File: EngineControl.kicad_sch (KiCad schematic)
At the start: 0 parts

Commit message: Complete Rev0
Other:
- added sheet Ignition (ignition.kicad_sch)
- added sheet MCU (mcu.kicad_sch)
- added sheet Power Delivery (power.kicad_sch)
- note added: "JLCPCB: JLC7628 Track Width Space Configuration DIFF90 6.89mil 4mil DIFF100 4.96mil 4mil DIFF120 4.97mil 8mil SE60 7.93mil N/A"
- company: (none) -> Badger
- title: (none) -> Badger-Pike: Engine Control Module

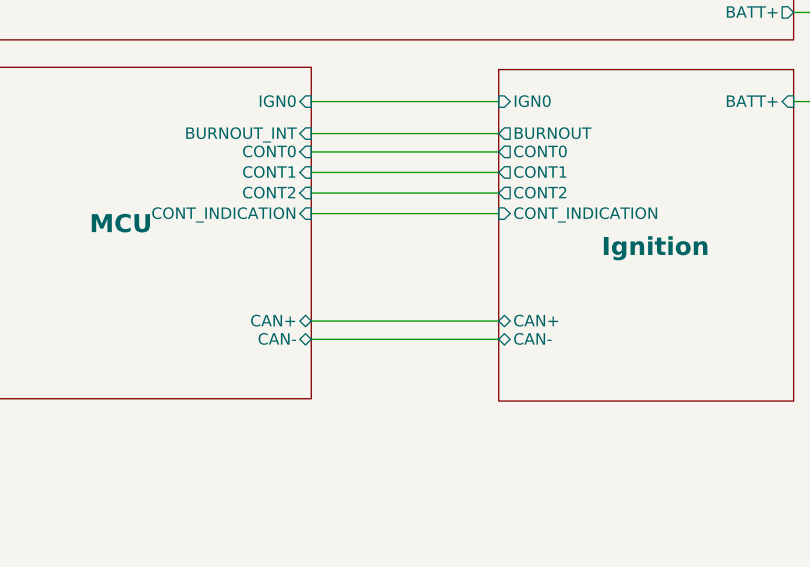
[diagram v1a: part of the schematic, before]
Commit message: Update ignition system with CDI
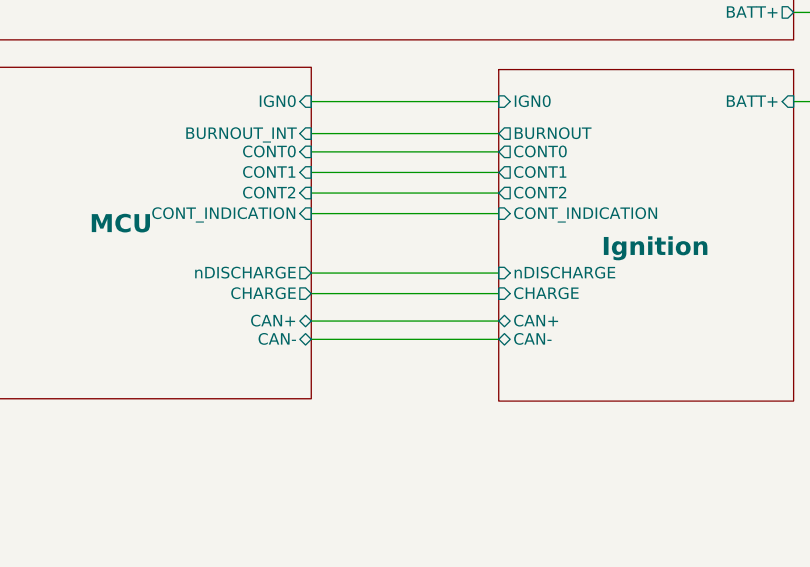
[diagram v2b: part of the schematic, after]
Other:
- sheet Ignition ports: added CHARGE, nDISCHARGE; removed none
- sheet MCU ports: added CHARGE, nDISCHARGE; removed none
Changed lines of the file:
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@@
+    (stroke (width 0) (type solid) (color 0 0 0 0))
+  )
+  (wire (pts (xy 142.24 77.47) (xy 163.068 77.47))
+    (stroke (width 0) (type solid) (color 0 0 0 0))
+  )
+  (wire (pts (xy 142.24 79.756) (xy 163.068 79.756))
     (stroke (width 0) (type solid) (color 0 0 0 0))
   )
@@
       (effects (font (size 1.27 1.27)) (justify left))
     )
+    (pin "nDISCHARGE" input (at 163.068 77.47 180)
+      (effects (font (size 1.27 1.27)) (justify left))
+    )
+    (pin "CHARGE" input (at 163.068 79.756 180)
+      (effects (font (size 1.27 1.27)) (justify left))
+    )
   )
   (sheet (at 102.108 54.61) (size 40.132 36.83)
@@
       (effects (font (size 1.27 1.27)) (justify right))
     )
+    (pin "nDISCHARGE" output (at 142.24 77.47 0)
+      (effects (font (size 1.27 1.27)) (justify right))
+    )
+    (pin "CHARGE" output (at 142.24 79.756 0)
+      (effects (font (size 1.27 1.27)) (justify right))
+    )
   )
   (sheet (at 101.854 34.544) (size 93.98 17.018)
@@
       (reference "#PWR021") (unit 1) (value "GND") (footprint "")
     )
+    (path "/021a2ddc-ba8f-4bf6-8fd4-c966327b4dd3/11e8ddb4-d444-4e7a-9a9e-5be1caf13b32"
+      (reference "#PWR?") (unit 1) (value "GND") (footprint "")
+    )
+    (path "/021a2ddc-ba8f-4bf6-8fd4-c966327b4dd3/169c89da-08f3-4afe-9e1c-06ef9693fbdb"
+      (reference "#PWR?") (unit 1) (value "GND") (footprint "")
+    )
+    (path "/021a2ddc-ba8f-4bf6-8fd4-c966327b4dd3/e03192f3-1f54-4a91-a410-de67ec52ca15"
+      (reference "#PWR?") (unit 1) (value "GND") (footprint "")
+    )
+    (path "/021a2ddc-ba8f-4bf6-8fd4-c966327b4dd3/fc22141e-0464-4c9b-a99c-9164e34aa44a"
+      (reference "#PWR?") (unit 1) (value "GND") (footprint "")
+    )
     (path "/472485e8-070c-45e8-970c-81997ac9d31f/9a635782-a656-4901-a321-decefa99a249"
       (reference "C1") (unit 1) (value "10uF") (footprint "Capacitor_Tantalum_SMD:CP_EIA-3216-18_Kemet-A")
@@
       (reference "C12") (unit 1) (value "100u") (footprint "Capacitor_Tantalum_SMD:CP_EIA-7343-31_Kemet-D")
     )
+    (path "/021a2ddc-ba8f-4bf6-8fd4-c966327b4dd3/e51a0524-21e2-417c-9e03-1e8f9e98a4c8"
+      (reference "C?") (unit 1) (value "2000uF") (footprint "")
+    )
     (path "/472485e8-070c-45e8-970c-81997ac9d31f/f9e04ee8-79d0-4648-81f5-c705e65b0835"
       (reference "D1") (unit 1) (value "LED_HeartBeat") (footprint "LED_SMD:LED_0603_1608Metric")
@@
       (reference "D3") (unit 1) (value "LED_Cont.") (footprint "LED_SMD:LED_0603_1608Metric")
     )
+    (path "/021a2ddc-ba8f-4bf6-8fd4-c966327b4dd3/529cc0e4-e45f-47f5-99e7-e39d73786a12"
+      (reference "D?") (unit 1) (value "LED_Charge") (footprint "LED_SMD:LED_0603_1608Metric")
+    )
+    (path "/021a2ddc-ba8f-4bf6-8fd4-c966327b4dd3/65e1a0d3-06ad-4d06-8248-bcd9e5015372"
+      (reference "D?") (unit 1) (value "LED_Discharge") (footprint "LED_SMD:LED_0603_1608Metric")
+    )
     (path "/472485e8-070c-45e8-970c-81997ac9d31f/f613bc73-f435-40ba-8cd6-0bc925e3ec73"
       (reference "FB1") (unit 1) (value "180 @ 100 Mhz") (footprint "Inductor_SMD:L_0603_1608Metric_Pad1.05x0.95mm_HandSolder")
@@
       (reference "L1") (unit 1) (value "4.7uH") (footprint "Inductor_SMD:L_Vishay_IHLP-1616")
     )
-    (path "/021a2ddc-ba8f-4bf6-8fd4-c966327b4dd3/f7481350-055a-4cee-b1b4-0fd602203b0e"
-      (reference "Q1") (unit 1) (value "Q_NMOS_GDS") (footprint "Package_TO_SOT_SMD:TO-263-3_TabPin2")
+    (path "/021a2ddc-ba8f-4bf6-8fd4-c966327b4dd3/9c8bf34f-46ee-48be-a480-69c389b9c0c8"
+      (reference "Q?") (unit 1) (value "Q_NMOS_GSD") (footprint "")
+    )
+    (path "/021a2ddc-ba8f-4bf6-8fd4-c966327b4dd3/f6891a3a-e048-46eb-bfc6-a9efdf878e9c"
+      (reference "Q?") (unit 1) (value "Q_NMOS_GSD") (footprint "")
     )
     (path "/472485e8-070c-45e8-970c-81997ac9d31f/6c7965de-69af-4ed2-ad27-cfe8a2e8bbc9"
@@
       (reference "R8") (unit 1) (value "1.5k") (footprint "Resistor_SMD:R_0402_1005Metric")
     )
-    (path "/021a2ddc-ba8f-4bf6-8fd4-c966327b4dd3/691f076b-c2f4-4e60-b380-21e64c3d310f"
-      (reference "R9") (unit 1) (value "220R") (footprint "Resistor_SMD:R_0402_1005Metric")
-    )
     (path "/021a2ddc-ba8f-4bf6-8fd4-c966327b4dd3/43e702a9-3533-4715-872a-827af84038be"
       (reference "R10") (unit 1) (value "1.5k") (footprint "Resistor_SMD:R_0402_1005Metric")
     )
+    (path "/021a2ddc-ba8f-4bf6-8fd4-c966327b4dd3/6f4b4f8f-5e59-4384-b394-dfa35396f290"
+      (reference "R?") (unit 1) (value "220R") (footprint "Resistor_SMD:R_0402_1005Metric")
+    )
+    (path "/021a2ddc-ba8f-4bf6-8fd4-c966327b4dd3/96c2e04e-9621-4953-811a-55f9cdbe47fe"
+      (reference "R?") (unit 1) (value "1.5k") (footprint "Resistor_SMD:R_0402_1005Metric")
+    )
+    (path "/021a2ddc-ba8f-4bf6-8fd4-c966327b4dd3/aa5dacce-ba6b-4ac3-8791-dce9d3bf9801"
+      (reference "R?") (unit 1) (value "220R") (footprint "Resistor_SMD:R_0402_1005Metric")
+    )
+    (path "/021a2ddc-ba8f-4bf6-8fd4-c966327b4dd3/e0571af3-4030-489e-8820-d86b2c375277"
+      (reference "R?") (unit 1) (value "1.5k") (footprint "Resistor_SMD:R_0402_1005Metric")
+    )
     (path "/472485e8-070c-45e8-970c-81997ac9d31f/e33953b3-4690-457f-b360-b7b9438ebddd"
       (reference "SW1") (unit 1) (value "BOOT") (footprint "Button_Switch_SMD:SW_DIP_SPSTx01_Slide_6.7x4.1mm_W6.73mm_P2.54mm_LowProfile_JPin")
@@
       (reference "U3") (unit 1) (value "AMS1117-3.3") (footprint "Package_TO_SOT_SMD:SOT-223-3_TabPin2")
     )
+    (path "/021a2ddc-ba8f-4bf6-8fd4-c966327b4dd3/e34a8f98-12ae-4dbb-a4e3-f354e5e27361"
+      (reference "U?") (unit 1) (value "CPC1135N") (footprint "Package_SO:SOP-4_3.8x4.1mm_P2.54mm")
+    )
     (path "/472485e8-070c-45e8-970c-81997ac9d31f/d4047988-d8c1-45f8-8d91-6d57e08950fe"

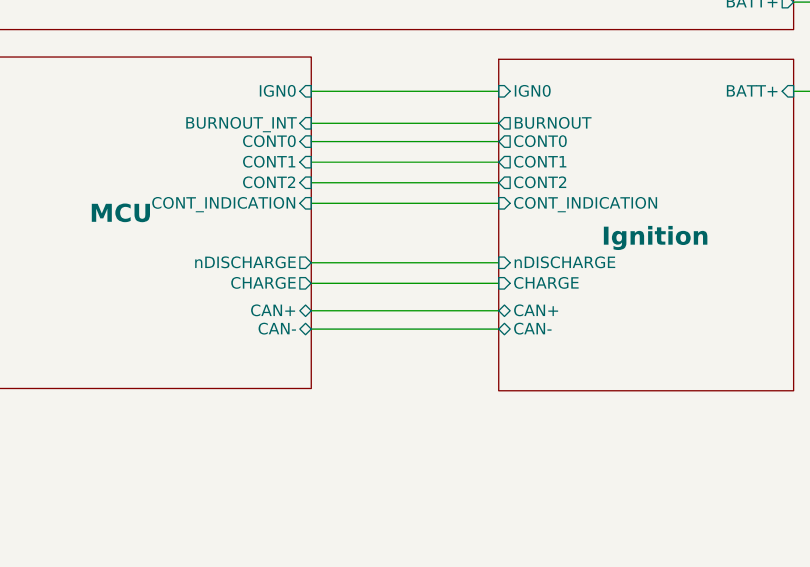
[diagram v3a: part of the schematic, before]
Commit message: #4 add pchannel for charge and nchannel for ignition
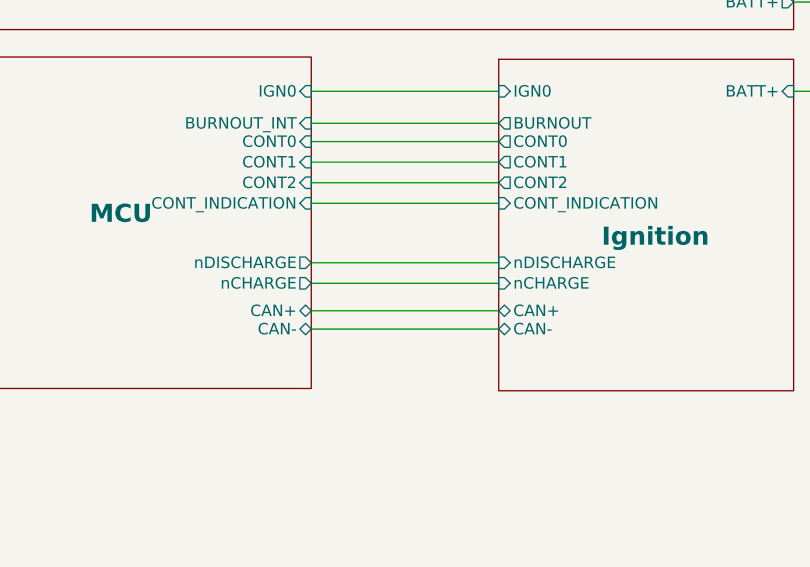
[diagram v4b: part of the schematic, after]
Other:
- sheet Ignition ports: added nCHARGE; removed CHARGE
- sheet MCU ports: added nCHARGE; removed CHARGE
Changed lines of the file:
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@@
       (effects (font (size 1.27 1.27)) (justify left))
     )
-    (pin "CHARGE" input (at 163.068 79.756 180)
+    (pin "nCHARGE" input (at 163.068 79.756 180)
       (effects (font (size 1.27 1.27)) (justify left))
     )
@@
       (effects (font (size 1.27 1.27)) (justify right))
     )
-    (pin "CHARGE" output (at 142.24 79.756 0)
+    (pin "nCHARGE" output (at 142.24 79.756 0)
       (effects (font (size 1.27 1.27)) (justify right))
     )
@@
       (reference "#PWR018") (unit 1) (value "GND") (footprint "")
     )
-    (path "/021a2ddc-ba8f-4bf6-8fd4-c966327b4dd3/66179501-8feb-443f-87b7-69728ec20e47"
+    (path "/021a2ddc-ba8f-4bf6-8fd4-c966327b4dd3/03958684-76a2-4a2e-904e-5f052f038332"
       (reference "#PWR019") (unit 1) (value "GND") (footprint "")
     )
@@
       (reference "#PWR021") (unit 1) (value "GND") (footprint "")
     )
-    (path "/021a2ddc-ba8f-4bf6-8fd4-c966327b4dd3/11e8ddb4-d444-4e7a-9a9e-5be1caf13b32"
-      (reference "#PWR022") (unit 1) (value "GND") (footprint "")
-    )
     (path "/021a2ddc-ba8f-4bf6-8fd4-c966327b4dd3/169c89da-08f3-4afe-9e1c-06ef9693fbdb"
       (reference "#PWR023") (unit 1) (value "GND") (footprint "")
@@
       (reference "L1") (unit 1) (value "4.7uH") (footprint "Inductor_SMD:L_Vishay_IHLP-1616")
     )
-    (path "/021a2ddc-ba8f-4bf6-8fd4-c966327b4dd3/f6891a3a-e048-46eb-bfc6-a9efdf878e9c"
-      (reference "Q1") (unit 1) (value "Q_NMOS_GSD") (footprint "Package_TO_SOT_SMD:SOT-23")
+    (path "/021a2ddc-ba8f-4bf6-8fd4-c966327b4dd3/b441a99b-7eb6-454c-8efc-1e30abb5c3e1"
+      (reference "Q1") (unit 1) (value "PMOS-GSD") (footprint "Package_TO_SOT_SMD:SOT-23")
     )
     (path "/021a2ddc-ba8f-4bf6-8fd4-c966327b4dd3/9c8bf34f-46ee-48be-a480-69c389b9c0c8"
@@
       (reference "R10") (unit 1) (value "1.5k") (footprint "Resistor_SMD:R_0402_1005Metric")
     )
-    (path "/021a2ddc-ba8f-4bf6-8fd4-c966327b4dd3/6f4b4f8f-5e59-4384-b394-dfa35396f290"
-      (reference "R11") (unit 1) (value "220R") (footprint "Resistor_SMD:R_0402_1005Metric")
+    (path "/021a2ddc-ba8f-4bf6-8fd4-c966327b4dd3/7158ea03-02b2-4ce0-90c1-0e3093223193"
+      (reference "R11") (unit 1) (value "100k") (footprint "")
     )
     (path "/021a2ddc-ba8f-4bf6-8fd4-c966327b4dd3/96c2e04e-9621-4953-811a-55f9cdbe47fe"
@@
       (reference "R13") (unit 1) (value "220R") (footprint "Resistor_SMD:R_0402_1005Metric")
     )
+    (path "/021a2ddc-ba8f-4bf6-8fd4-c966327b4dd3/1c8d51e0-1f2b-4f95-85d6-d9e259006f9d"
+      (reference "R14") (unit 1) (value "1.5k") (footprint "Resistor_SMD:R_0402_1005Metric")
+    )
     (path "/472485e8-070c-45e8-970c-81997ac9d31f/e33953b3-4690-457f-b360-b7b9438ebddd"

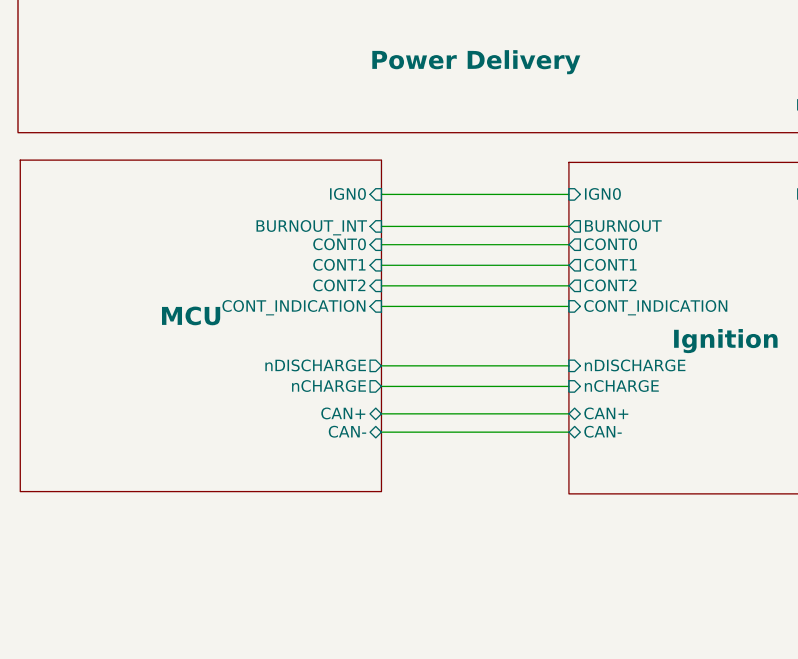
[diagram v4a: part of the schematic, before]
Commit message: #1 New pyro channel introduced in schematic
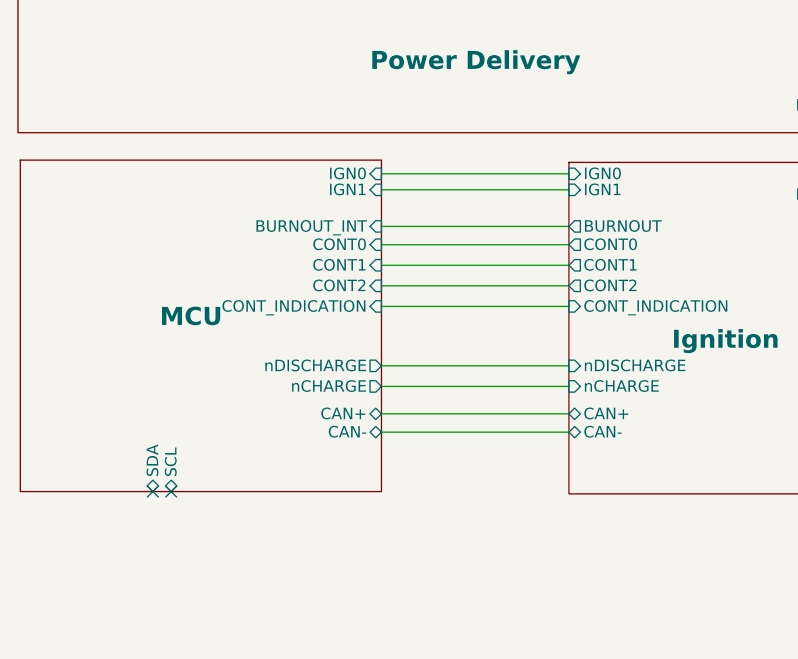
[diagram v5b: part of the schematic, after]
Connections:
- no-connect marks 0 -> 2
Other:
- sheet Ignition ports: added IGN1; removed none
- sheet MCU ports: added IGN1, SCL, SDA; removed none
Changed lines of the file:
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@@
     (company "Badger")
   )
-  (wire (pts (xy 142.24 58.42) (xy 163.068 58.42))
+  (no_connect (at 116.84 91.44))
+  (no_connect (at 118.872 91.44))
+  (wire (pts (xy 142.24 56.134) (xy 163.068 56.134))
+    (stroke (width 0) (type solid) (color 0 0 0 0))
+  )
+  (wire (pts (xy 142.24 57.912) (xy 163.068 57.912))
     (stroke (width 0) (type solid) (color 0 0 0 0))
   )
@@
       (effects (font (size 1.27 1.27)) (justify right))
     )
-    (pin "IGN0" input (at 163.068 58.42 180)
+    (pin "IGN0" input (at 163.068 56.134 180)
       (effects (font (size 1.27 1.27)) (justify left))
     )
@@
     )
     (pin "nCHARGE" input (at 163.068 79.756 180)
+      (effects (font (size 1.27 1.27)) (justify left))
+    )
+    (pin "IGN1" input (at 163.068 57.912 180)
       (effects (font (size 1.27 1.27)) (justify left))
     )
@@
       (effects (font (size 1.27 1.27)) (justify right))
     )
-    (pin "IGN0" input (at 142.24 58.42 0)
+    (pin "IGN0" input (at 142.24 56.134 0)
       (effects (font (size 1.27 1.27)) (justify right))
     )
@@
     )
     (pin "nCHARGE" output (at 142.24 79.756 0)
+      (effects (font (size 1.27 1.27)) (justify right))
+    )
+    (pin "SDA" bidirectional (at 116.84 91.44 270)
+      (effects (font (size 1.27 1.27)) (justify left))
+    )
+    (pin "SCL" bidirectional (at 118.872 91.44 270)
+      (effects (font (size 1.27 1.27)) (justify left))
+    )
+    (pin "IGN1" input (at 142.24 57.912 0)
       (effects (font (size 1.27 1.27)) (justify right))
     )
@@
       (reference "#PWR025") (unit 1) (value "GND") (footprint "")
     )
+    (path "/021a2ddc-ba8f-4bf6-8fd4-c966327b4dd3/4aeaac5a-2cde-4037-9e7a-5c1c4b1275d0"
+      (reference "#PWR?") (unit 1) (value "GND") (footprint "")
+    )
     (path "/472485e8-070c-45e8-970c-81997ac9d31f/9a635782-a656-4901-a321-decefa99a249"
       (reference "C1") (unit 1) (value "10uF") (footprint "Capacitor_Tantalum_SMD:CP_EIA-3216-18_Kemet-A")
@@
       (reference "J7") (unit 1) (value "GPIO") (footprint "Connector_PinHeader_2.54mm:PinHeader_1x04_P2.54mm_Vertical")
     )
+    (path "/021a2ddc-ba8f-4bf6-8fd4-c966327b4dd3/2a45d4d6-52b7-4a1b-861f-6806ea44ed57"
+      (reference "J?") (unit 1) (value "PYRO1") (footprint "")
+    )
     (path "/88e3204c-6dd4-4bca-8d93-a1bae11ba17d/f9b839d5-4af8-426d-87ab-2df2d53ead01"
       (reference "L1") (unit 1) (value "4.7uH") (footprint "Inductor_SMD:L_Vishay_IHLP-1616")
@@
       (reference "Q2") (unit 1) (value "Q_NMOS_GSD") (footprint "Package_TO_SOT_SMD:SOT-23")
     )
+    (path "/021a2ddc-ba8f-4bf6-8fd4-c966327b4dd3/a79d2ddf-9434-4c89-a58c-488151bf3b66"
+      (reference "Q?") (unit 1) (value "Q_NMOS_GSD") (footprint "Package_TO_SOT_SMD:SOT-23")
+    )
     (path "/472485e8-070c-45e8-970c-81997ac9d31f/6c7965de-69af-4ed2-ad27-cfe8a2e8bbc9"
       (reference "R1") (unit 1) (value "1.5k") (footprint "Resistor_SMD:R_0402_1005Metric")
@@
       (reference "R14") (unit 1) (value "1.5k") (footprint "Resistor_SMD:R_0402_1005Metric")
     )
+    (path "/021a2ddc-ba8f-4bf6-8fd4-c966327b4dd3/300818aa-bcb1-40d6-89b2-9439f11ce4ba"
+      (reference "R?") (unit 1) (value "220R") (footprint "Resistor_SMD:R_0402_1005Metric")
+    )
     (path "/472485e8-070c-45e8-970c-81997ac9d31f/e33953b3-4690-457f-b360-b7b9438ebddd"
